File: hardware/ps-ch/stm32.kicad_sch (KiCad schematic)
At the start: 17 parts, among them J1 Conn_02x05_Odd_Even, U12 STM32C031K4Tx

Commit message: first pcb sync
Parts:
- removed J1: Conn_02x05_Odd_Even, symbol Connector_Generic:Conn_02x05_Odd_Even
- added J3: Conn_01x05, Connector_PinHeader_2.54mm:PinHeader_1x05_P2.54mm_Vertical, symbol Connector_Generic:Conn_01x05
- renumbered C60 to C58, C54 to C59, C55 to C60, R64 to R39, R45 to R40, R55 to R41, R84 to R42, R83 to R43, R36 to R44, R38 to R45, R49 to R46, R60 to R47, R35 to R48, U12 to U10
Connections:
- net +3V3: now also J3.1 (Pin_1)
- net ACTIVATE_BOOTLOADER: now also J3.2 (Pin_2)
- net GND: now also J3.3 (Pin_3)
- net NRST: now also J3.5 (Pin_5)
- net SWDIO: now also J3.4 (Pin_4)

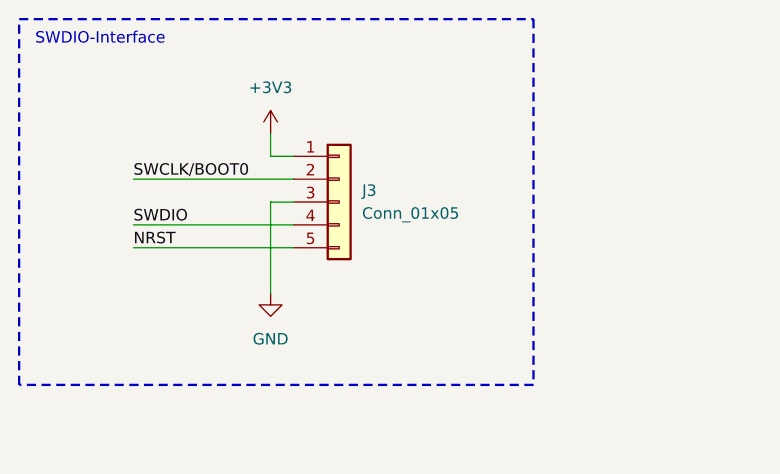
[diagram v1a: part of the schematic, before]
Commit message: removed cmc, replaced input/output connectors
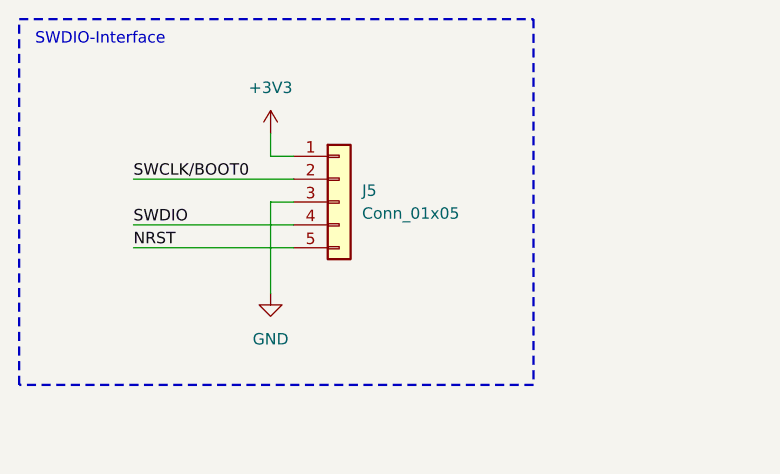
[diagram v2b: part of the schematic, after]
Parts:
- renumbered J3 to J5
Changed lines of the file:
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@@
 		(dnp no)
 		(fields_autoplaced yes)
-		(property "Reference" "#PWR0112"
+		(property "Reference" "#PWR0110"
 			(at 138.43 154.94 0)
 			(effects
@@
 			(project "ps-ch"
 				(path "/431acd2e-2ab9-4aa9-b759-273f044decc5/2d82f172-f8c7-4db1-beb9-4320019db4fa"
-					(reference "#PWR0112")
+					(reference "#PWR0110")
 					(unit 1)
 				)
@@
 		(on_board yes)
 		(dnp no)
-		(property "Reference" "#PWR0111"
+		(property "Reference" "#PWR0109"
 			(at 138.43 137.16 0)
 			(effects
@@
 			(project "ps-ch"
 				(path "/431acd2e-2ab9-4aa9-b759-273f044decc5/2d82f172-f8c7-4db1-beb9-4320019db4fa"
-					(reference "#PWR0111")
+					(reference "#PWR0109")
 					(unit 1)
 				)
@@
 		(dnp no)
 		(fields_autoplaced yes)
-		(property "Reference" "#PWR0109"
+		(property "Reference" "#PWR0107"
 			(at 143.51 123.19 0)
 			(effects
@@
 			(project "ps-ch"
 				(path "/431acd2e-2ab9-4aa9-b759-273f044decc5/2d82f172-f8c7-4db1-beb9-4320019db4fa"
-					(reference "#PWR0109")
+					(reference "#PWR0107")
 					(unit 1)
 				)
@@
 		(dnp no)
 		(fields_autoplaced yes)
-		(property "Reference" "#PWR0101"
+		(property "Reference" "#PWR099"
 			(at 45.72 34.29 0)
 			(effects
@@
 			(project "ps-ch"
 				(path "/431acd2e-2ab9-4aa9-b759-273f044decc5/2d82f172-f8c7-4db1-beb9-4320019db4fa"
-					(reference "#PWR0101")
+					(reference "#PWR099")
 					(unit 1)
 				)
@@
 		(dnp no)
 		(fields_autoplaced yes)
-		(property "Reference" "#PWR0105"
+		(property "Reference" "#PWR0103"
 			(at 179.07 57.15 0)
 			(effects
@@
 			(project "ps-ch"
 				(path "/431acd2e-2ab9-4aa9-b759-273f044decc5/2d82f172-f8c7-4db1-beb9-4320019db4fa"
-					(reference "#PWR0105")
+					(reference "#PWR0103")
 					(unit 1)
 				)
@@
 		(dnp no)
 		(fields_autoplaced yes)
-		(property "Reference" "#PWR0113"
+		(property "Reference" "#PWR0111"
 			(at 148.59 154.94 0)
 			(effects
@@
 			(project "ps-ch"
 				(path "/431acd2e-2ab9-4aa9-b759-273f044decc5/2d82f172-f8c7-4db1-beb9-4320019db4fa"
-					(reference "#PWR0113")
+					(reference "#PWR0111")
 					(unit 1)
 				)
@@
 		(dnp no)
 		(fields_autoplaced yes)
-		(property "Reference" "#PWR0110"
+		(property "Reference" "#PWR0108"
 			(at 156.21 123.19 0)
 			(effects
@@
 			(project "ps-ch"
 				(path "/431acd2e-2ab9-4aa9-b759-273f044decc5/2d82f172-f8c7-4db1-beb9-4320019db4fa"
-					(reference "#PWR0110")
+					(reference "#PWR0108")
 					(unit 1)
 				)
@@
 		(dnp no)
 		(fields_autoplaced yes)
-		(property "Reference" "#PWR0104"
+		(property "Reference" "#PWR0102"
 			(at 168.91 57.15 0)
 			(effects
@@
 			(project "ps-ch"
 				(path "/431acd2e-2ab9-4aa9-b759-273f044decc5/2d82f172-f8c7-4db1-beb9-4320019db4fa"
-					(reference "#PWR0104")
+					(reference "#PWR0102")
 					(unit 1)
 				)
@@
 		(dnp no)
 		(fields_autoplaced yes)
-		(property "Reference" "#PWR0102"
+		(property "Reference" "#PWR0100"
 			(at 45.72 54.61 0)
 			(effects
@@
 			(project "ps-ch"
 				(path "/431acd2e-2ab9-4aa9-b759-273f044decc5/2d82f172-f8c7-4db1-beb9-4320019db4fa"
-					(reference "#PWR0102")
+					(reference "#PWR0100")
 					(unit 1)
 				)
@@
 		(dnp no)
 		(fields_autoplaced yes)
-		(property "Reference" "#PWR0108"
+		(property "Reference" "#PWR0106"
 			(at 130.81 123.19 0)
 			(effects
@@
 			(project "ps-ch"
 				(path "/431acd2e-2ab9-4aa9-b759-273f044decc5/2d82f172-f8c7-4db1-beb9-4320019db4fa"
-					(reference "#PWR0108")
+					(reference "#PWR0106")
 					(unit 1)
 				)
@@
 		(dnp no)
 		(fields_autoplaced yes)
-		(property "Reference" "J3"
+		(property "Reference" "J5"
 			(at 55.88 36.8299 0)
 			(effects
@@
 			(project "ps-ch"
 				(path "/431acd2e-2ab9-4aa9-b759-273f044decc5/2d82f172-f8c7-4db1-beb9-4320019db4fa"
-					(reference "J3")
+					(reference "J5")
 					(unit 1)
 				)
@@
 		(dnp no)
 		(fields_autoplaced yes)
-		(property "Reference" "#PWR0107"
+		(property "Reference" "#PWR0105"
 			(at 215.9 85.09 0)
 			(effects
@@
 			(project "ps-ch"
 				(path "/431acd2e-2ab9-4aa9-b759-273f044decc5/2d82f172-f8c7-4db1-beb9-4320019db4fa"
-					(reference "#PWR0107")
+					(reference "#PWR0105")
 					(unit 1)
 				)
@@
 		(dnp no)
 		(fields_autoplaced yes)
-		(property "Reference" "#PWR0106"
+		(property "Reference" "#PWR0104"
 			(at 215.9 57.15 0)
 			(effects
@@
 			(project "ps-ch"
 				(path "/431acd2e-2ab9-4aa9-b759-273f044decc5/2d82f172-f8c7-4db1-beb9-4320019db4fa"
-					(reference "#PWR0106")
+					(reference "#PWR0104")
 					(unit 1)
 				)
@@
 		(dnp no)
 		(fields_autoplaced yes)
-		(property "Reference" "#PWR0103"
+		(property "Reference" "#PWR0101"
 			(at 143.51 57.15 0)
 			(effects
@@
 			(project "ps-ch"
 				(path "/431acd2e-2ab9-4aa9-b759-273f044decc5/2d82f172-f8c7-4db1-beb9-4320019db4fa"
-					(reference "#PWR0103")
-					(unit 1)
-				)
+					(reference "#PWR0101")
+					(unit 1)
+				)
